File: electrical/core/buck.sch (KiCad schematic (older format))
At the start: 0 parts

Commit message: Size SEPIC inductor and MOSFETs
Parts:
- added L1: 15u, symbol Device:L
- added Q3, Q4: IRF540N, Package_TO_SOT_THT:TO-220-3_Vertical, symbol Transistor_FET:IRF540N
- added U5: LM5118, Package_SO:HTSSOP-20-1EP_4.4x6.5mm_P0.65mm_EP3.4x6.5mm, symbol rasbot:LM5118
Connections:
- new net: Q4.1 (G), U5.15 (LO)
- new net: Q3.1 (G), U5.19 (HO)
- new net: L1.1, Q3.3 (S), U5.20 (HS)
- new net: L1.2, Q4.2 (D)
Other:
- note added: "SEPIC"
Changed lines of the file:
@@
 Comment4 ""
 $EndDescr
+Text Notes 2650 2850 0    100  ~ 20
+SEPIC
+$Comp
+L rasbot:LM5118 U5
+U 1 1 5D54082F
+P 2700 4100
+F 0 "U5" H 2700 4993 100 0000 C CNN
+F 1 "LM5118" H 2700 4827 100 0000 C CNN
+F 2 "Package_SO:HTSSOP-20-1EP_4.4x6.5mm_P0.65mm_EP3.4x6.5mm" H 2600 4000 100 0001 C CNN
+F 3 "http://www.ti.com/lit/ds/symlink/lm5118.pdf" H 2600 4000 100 0001 C CNN
+	1    2700 4100
+	1    0    0    -1
+$EndComp
+$Comp
+L Transistor_FET:IRF540N Q4
+U 1 1 5D541C10
+P 4750 4400
+F 0 "Q4" H 4956 4446 50  0000 L CNN
+F 1 "IRF540N" H 4956 4355 50  0000 L CNN
+F 2 "Package_TO_SOT_THT:TO-220-3_Vertical" H 5000 4325 50  0001 L CIN
+F 3 "http://www.irf.com/product-info/datasheets/data/irf540n.pdf" H 4750 4400 50  0001 L CNN
+	1    4750 4400
+	1    0    0    -1
+$EndComp
+Wire Wire Line
+	4550 4400 3200 4400
+Wire Wire Line
+	3200 4000 3250 4000
+$Comp
+L Device:L L1
+U 1 1 5D54429F
+P 4600 4100
+F 0 "L1" V 4790 4100 50  0000 C CNN
+F 1 "15u" V 4699 4100 50  0000 C CNN
+F 2 "" H 4600 4100 50  0001 C CNN
+F 3 "~" H 4600 4100 50  0001 C CNN
+	1    4600 4100
+	0    -1   -1   0
+$EndComp
+Wire Wire Line
+	4750 4100 4850 4100
+Wire Wire Line
+	4850 4100 4850 4200
+Wire Wire Line
+	3250 4000 3250 4100
+Connection ~ 4000 4100
+Wire Wire Line
+	3250 4100 4000 4100
+Wire Wire Line
+	4450 4100 4000 4100
+Wire Wire Line
+	3700 3900 3200 3900
+$Comp
+L Transistor_FET:IRF540N Q3
+U 1 1 5D54261D
+P 3900 3900
+F 0 "Q3" H 4106 3946 50  0000 L CNN
+F 1 "IRF540N" H 4106 3855 50  0000 L CNN
+F 2 "Package_TO_SOT_THT:TO-220-3_Vertical" H 4150 3825 50  0001 L CIN
+F 3 "http://www.irf.com/product-info/datasheets/data/irf540n.pdf" H 3900 3900 50  0001 L CNN
+	1    3900 3900
+	1    0    0    -1
+$EndComp
 $EndSCHEMATC

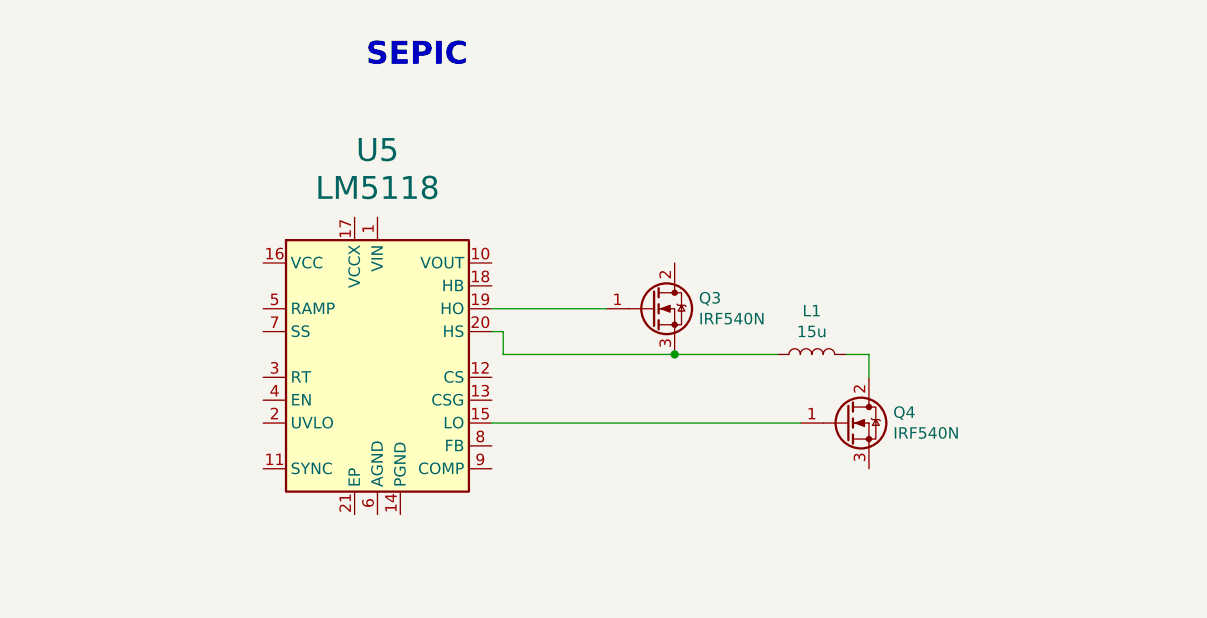
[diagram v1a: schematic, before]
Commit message: Fix division in power
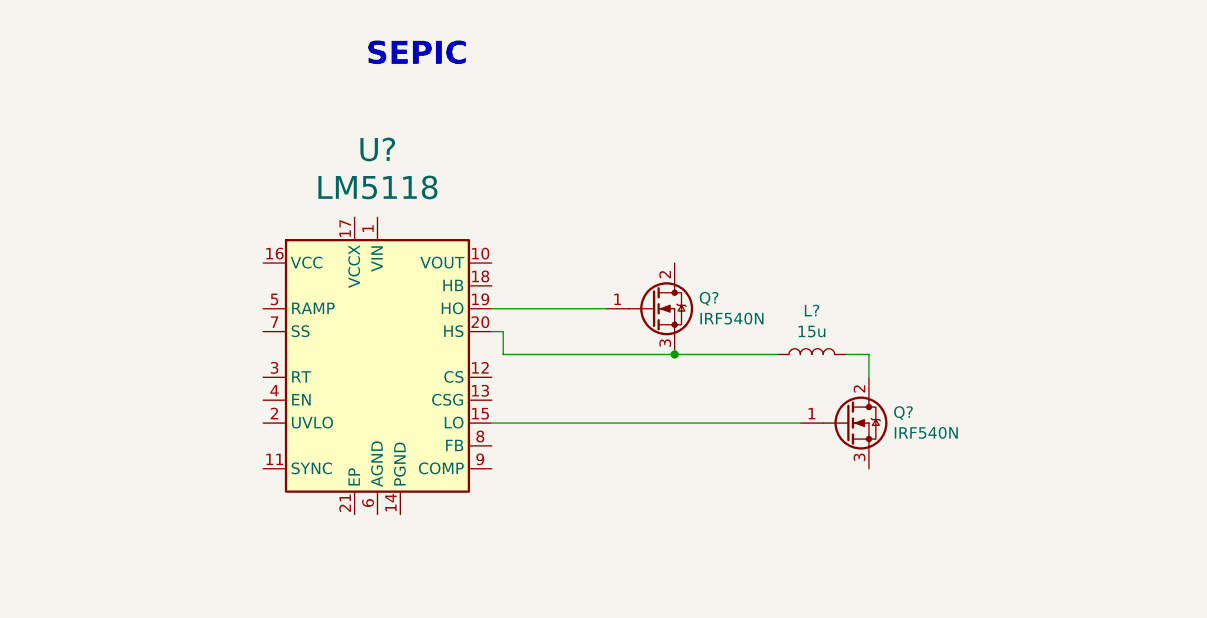
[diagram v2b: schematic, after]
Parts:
- renumbered L1 to L?, Q4 to Q?, Q3 to Q?, U5 to U?
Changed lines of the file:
@@
 SEPIC
 $Comp
-L rasbot:LM5118 U5
+L rasbot:LM5118 U?
 U 1 1 5D54082F
 P 2700 4100
-F 0 "U5" H 2700 4993 100 0000 C CNN
+F 0 "U?" H 2700 4993 100 0000 C CNN
 F 1 "LM5118" H 2700 4827 100 0000 C CNN
 F 2 "Package_SO:HTSSOP-20-1EP_4.4x6.5mm_P0.65mm_EP3.4x6.5mm" H 2600 4000 100 0001 C CNN
@@
 $EndComp
 $Comp
-L Transistor_FET:IRF540N Q4
+L Transistor_FET:IRF540N Q?
 U 1 1 5D541C10
 P 4750 4400
-F 0 "Q4" H 4956 4446 50  0000 L CNN
+F 0 "Q?" H 4956 4446 50  0000 L CNN
 F 1 "IRF540N" H 4956 4355 50  0000 L CNN
 F 2 "Package_TO_SOT_THT:TO-220-3_Vertical" H 5000 4325 50  0001 L CIN
@@
 	3200 4000 3250 4000
 $Comp
-L Device:L L1
+L Device:L L?
 U 1 1 5D54429F
 P 4600 4100
-F 0 "L1" V 4790 4100 50  0000 C CNN
+F 0 "L?" V 4790 4100 50  0000 C CNN
 F 1 "15u" V 4699 4100 50  0000 C CNN
 F 2 "" H 4600 4100 50  0001 C CNN
@@
 	3700 3900 3200 3900
 $Comp
-L Transistor_FET:IRF540N Q3
+L Transistor_FET:IRF540N Q?
 U 1 1 5D54261D
 P 3900 3900
-F 0 "Q3" H 4106 3946 50  0000 L CNN
+F 0 "Q?" H 4106 3946 50  0000 L CNN
 F 1 "IRF540N" H 4106 3855 50  0000 L CNN
 F 2 "Package_TO_SOT_THT:TO-220-3_Vertical" H 4150 3825 50  0001 L CIN

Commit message: Supply and Enable
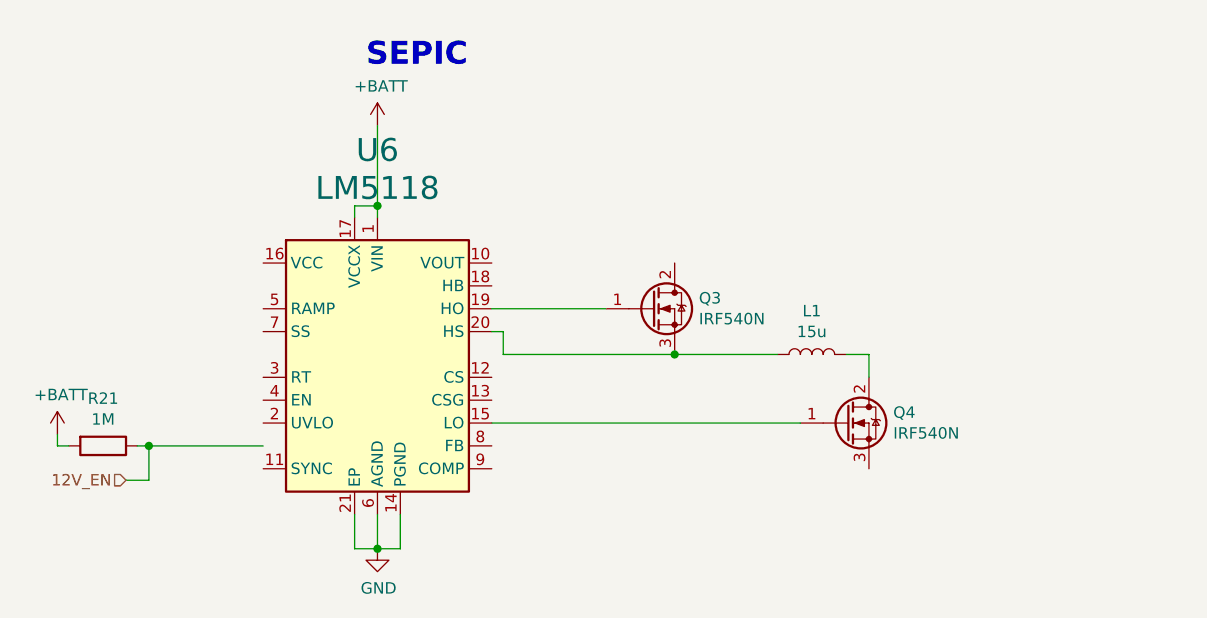
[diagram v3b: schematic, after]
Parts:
- added R21: 1M, symbol Device:R
- gave numbers to parts that had none: 4
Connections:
- net labels added: +BATT, 12V_EN, GND
- wire segments 8 -> 23
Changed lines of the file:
@@
 SEPIC
 $Comp
-L rasbot:LM5118 U?
+L rasbot:LM5118 U6
 U 1 1 5D54082F
 P 2700 4100
-F 0 "U?" H 2700 4993 100 0000 C CNN
+F 0 "U6" H 2700 4993 100 0000 C CNN
 F 1 "LM5118" H 2700 4827 100 0000 C CNN
 F 2 "Package_SO:HTSSOP-20-1EP_4.4x6.5mm_P0.65mm_EP3.4x6.5mm" H 2600 4000 100 0001 C CNN
@@
 $EndComp
 $Comp
-L Transistor_FET:IRF540N Q?
+L Transistor_FET:IRF540N Q4
 U 1 1 5D541C10
 P 4750 4400
-F 0 "Q?" H 4956 4446 50  0000 L CNN
+F 0 "Q4" H 4956 4446 50  0000 L CNN
 F 1 "IRF540N" H 4956 4355 50  0000 L CNN
 F 2 "Package_TO_SOT_THT:TO-220-3_Vertical" H 5000 4325 50  0001 L CIN
@@
 	3200 4000 3250 4000
 $Comp
-L Device:L L?
+L Device:L L1
 U 1 1 5D54429F
 P 4600 4100
-F 0 "L?" V 4790 4100 50  0000 C CNN
+F 0 "L1" V 4790 4100 50  0000 C CNN
 F 1 "15u" V 4699 4100 50  0000 C CNN
 F 2 "" H 4600 4100 50  0001 C CNN
@@
 	3700 3900 3200 3900
 $Comp
-L Transistor_FET:IRF540N Q?
+L Transistor_FET:IRF540N Q3
 U 1 1 5D54261D
 P 3900 3900
-F 0 "Q?" H 4106 3946 50  0000 L CNN
+F 0 "Q3" H 4106 3946 50  0000 L CNN
 F 1 "IRF540N" H 4106 3855 50  0000 L CNN
 F 2 "Package_TO_SOT_THT:TO-220-3_Vertical" H 4150 3825 50  0001 L CIN
@@
 	1    0    0    -1
 $EndComp
+$Comp
+L power:+BATT #PWR?
+U 1 1 5DA92B89
+P 2700 3100
+AR Path="/5D48851F/5DA878D9/5DA92B89" Ref="#PWR?"  Part="1"
+AR Path="/5D48851F/5DA8C423/5DA92B89" Ref="#PWR051"  Part="1"
+F 0 "#PWR051" H 2700 2950 50  0001 C CNN
+F 1 "+BATT" H 2715 3273 50  0000 C CNN
+F 2 "" H 2700 3100 50  0001 C CNN
+F 3 "" H 2700 3100 50  0001 C CNN
+	1    2700 3100
+	1    0    0    -1
+$EndComp
+Wire Wire Line
+	2700 3100 2700 3450
+Wire Wire Line
+	2700 3450 2600 3450
+Wire Wire Line
+	2600 3450 2600 3500
+Connection ~ 2700 3450
+Wire Wire Line
+	2700 3450 2700 3500
+$Comp
+L power:GND #PWR052
+U 1 1 5DA9483F
+P 2700 4950
+F 0 "#PWR052" H 2700 4700 50  0001 C CNN
+F 1 "GND" H 2705 4777 50  0000 C CNN
+F 2 "" H 2700 4950 50  0001 C CNN
+F 3 "" H 2700 4950 50  0001 C CNN
+	1    2700 4950
+	1    0    0    -1
+$EndComp
+Wire Wire Line
+	2700 4950 2600 4950
+Wire Wire Line
+	2600 4950 2600 4800
+Wire Wire Line
+	2700 4950 2800 4950
+Wire Wire Line
+	2800 4950 2800 4800
+Connection ~ 2700 4950
+Wire Wire Line
+	2700 4950 2700 4800
+$Comp
+L Device:R R21
+U 1 1 5DA95D12
+P 1500 4500
+F 0 "R21" V 1293 4500 50  0000 C CNN
+F 1 "1M" V 1384 4500 50  0000 C CNN
+F 2 "" V 1430 4500 50  0001 C CNN
+F 3 "~" H 1500 4500 50  0001 C CNN
+	1    1500 4500
+	0    1    1    0
+$EndComp
+$Comp
+L power:+BATT #PWR?
+U 1 1 5DA97039
+P 1300 4450
+AR Path="/5D48851F/5DA878D9/5DA97039" Ref="#PWR?"  Part="1"
+AR Path="/5D48851F/5DA8C423/5DA97039" Ref="#PWR050"  Part="1"
+F 0 "#PWR050" H 1300 4300 50  0001 C CNN
+F 1 "+BATT" H 1315 4623 50  0000 C CNN
+F 2 "" H 1300 4450 50  0001 C CNN
+F 3 "" H 1300 4450 50  0001 C CNN
+	1    1300 4450
+	1    0    0    -1
+$EndComp
+Wire Wire Line
+	1300 4450 1300 4500
+Wire Wire Line
+	1300 4500 1350 4500
+Wire Wire Line
+	1650 4500 1700 4500
+Text HLabel 1600 4650 0    50   Input ~ 0
+12V_EN
+Wire Wire Line
+	1600 4650 1700 4650
+Wire Wire Line
+	1700 4650 1700 4500
+Connection ~ 1700 4500
+Wire Wire Line
+	1700 4500 2200 4500
 $EndSCHEMATC

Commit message: Inductor Footprint
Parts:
- L1: footprint (none) -> Inductor_SMD:L_10.4x10.4_H4.8
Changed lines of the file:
@@
 F 0 "L1" V 4790 4100 50  0000 C CNN
 F 1 "15u" V 4699 4100 50  0000 C CNN
-F 2 "" H 4600 4100 50  0001 C CNN
+F 2 "Inductor_SMD:L_10.4x10.4_H4.8" H 4600 4100 50  0001 C CNN
 F 3 "~" H 4600 4100 50  0001 C CNN
 	1    4600 4100

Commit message: MOSFET Footprint
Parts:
- Q3, Q4: footprint Package_TO_SOT_THT:TO-220-3_Vertical -> Package_TO_SOT_SMD:TO-263-2
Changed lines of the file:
@@
 F 0 "Q4" H 4956 4446 50  0000 L CNN
 F 1 "IRF540N" H 4956 4355 50  0000 L CNN
-F 2 "Package_TO_SOT_THT:TO-220-3_Vertical" H 5000 4325 50  0001 L CIN
+F 2 "Package_TO_SOT_SMD:TO-263-2" H 5000 4325 50  0001 L CIN
 F 3 "http://www.irf.com/product-info/datasheets/data/irf540n.pdf" H 4750 4400 50  0001 L CNN
 	1    4750 4400
@@
 F 0 "Q3" H 4106 3946 50  0000 L CNN
 F 1 "IRF540N" H 4106 3855 50  0000 L CNN
-F 2 "Package_TO_SOT_THT:TO-220-3_Vertical" H 4150 3825 50  0001 L CIN
+F 2 "Package_TO_SOT_SMD:TO-263-2" H 4150 3825 50  0001 L CIN
 F 3 "http://www.irf.com/product-info/datasheets/data/irf540n.pdf" H 3900 3900 50  0001 L CNN
 	1    3900 3900

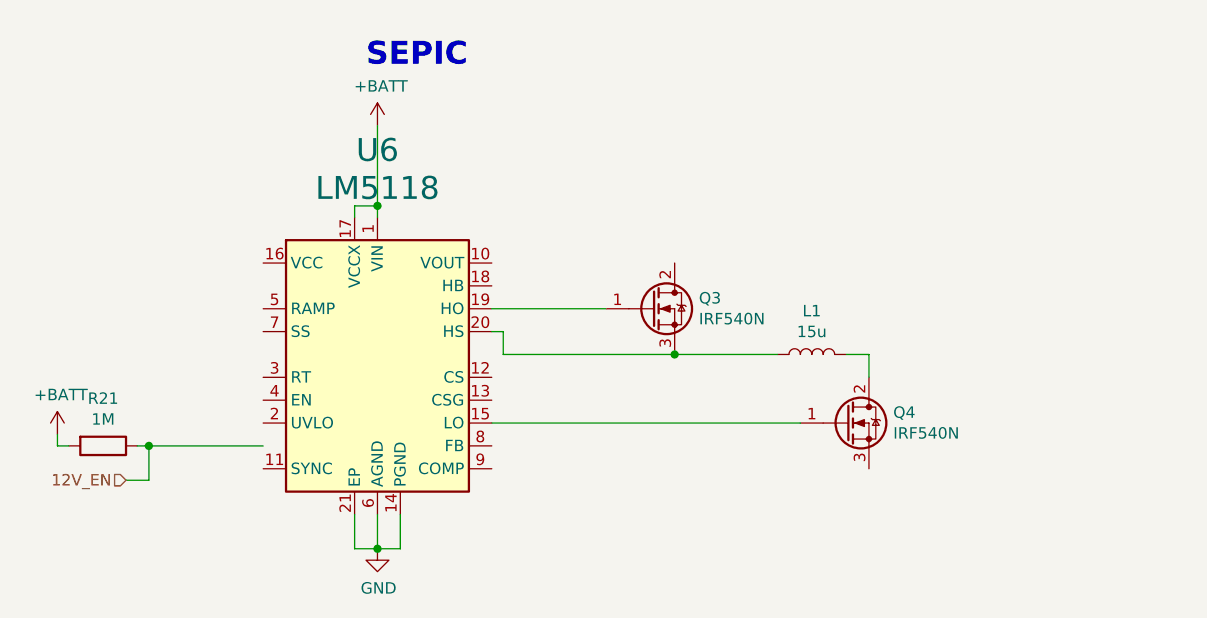
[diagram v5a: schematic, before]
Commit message: SEPIC rectify output
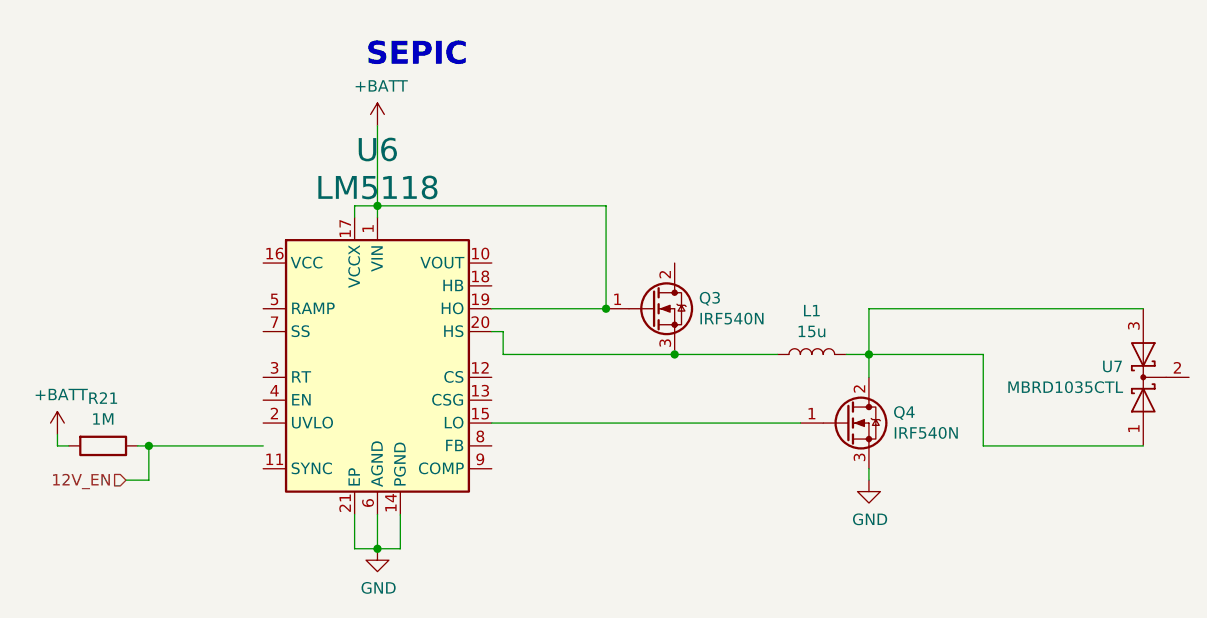
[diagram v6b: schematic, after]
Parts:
- added U7: MBRD1035CTL, symbol rasbot:MBRD1035CTL
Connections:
- wire segments 23 -> 31
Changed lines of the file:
@@
 Wire Wire Line
 	4450 4100 4000 4100
-Wire Wire Line
-	3700 3900 3200 3900
 $Comp
 L Transistor_FET:IRF540N Q3
@@
 Wire Wire Line
 	2700 3100 2700 3450
-Wire Wire Line
-	2700 3450 2600 3450
-Wire Wire Line
-	2600 3450 2600 3500
 Connection ~ 2700 3450
 Wire Wire Line
@@
 Wire Wire Line
 	1700 4500 2200 4500
+Wire Wire Line
+	3700 3900 3700 3450
+Wire Wire Line
+	3700 3450 2700 3450
+Connection ~ 3700 3900
+Wire Wire Line
+	3700 3900 3200 3900
+$Comp
+L power:GND #PWR053
+U 1 1 5DAA46C0
+P 4850 4650
+F 0 "#PWR053" H 4850 4400 50  0001 C CNN
+F 1 "GND" H 4855 4477 50  0000 C CNN
+F 2 "" H 4850 4650 50  0001 C CNN
+F 3 "" H 4850 4650 50  0001 C CNN
+	1    4850 4650
+	1    0    0    -1
+$EndComp
+Wire Wire Line
+	4850 4650 4850 4600
+Wire Wire Line
+	2600 3450 2600 3500
+Wire Wire Line
+	2700 3450 2600 3450
+$Comp
+L rasbot:MBRD1035CTL U7
+U 1 1 5DAAF97C
+P 6050 4200
+F 0 "U7" V 6096 4288 50  0000 L CNN
+F 1 "MBRD1035CTL" V 6005 4288 50  0000 L CNN
+F 2 "" H 6050 4200 50  0001 C CNN
+F 3 "" H 6050 4200 50  0001 C CNN
+	1    6050 4200
+	0    -1   -1   0
+$EndComp
+Wire Wire Line
+	6050 3900 4850 3900
+Wire Wire Line
+	4850 3900 4850 4100
+Connection ~ 4850 4100
+Wire Wire Line
+	6050 4500 5350 4500
+Wire Wire Line
+	5350 4500 5350 4100
+Wire Wire Line
+	5350 4100 4850 4100
 $EndSCHEMATC

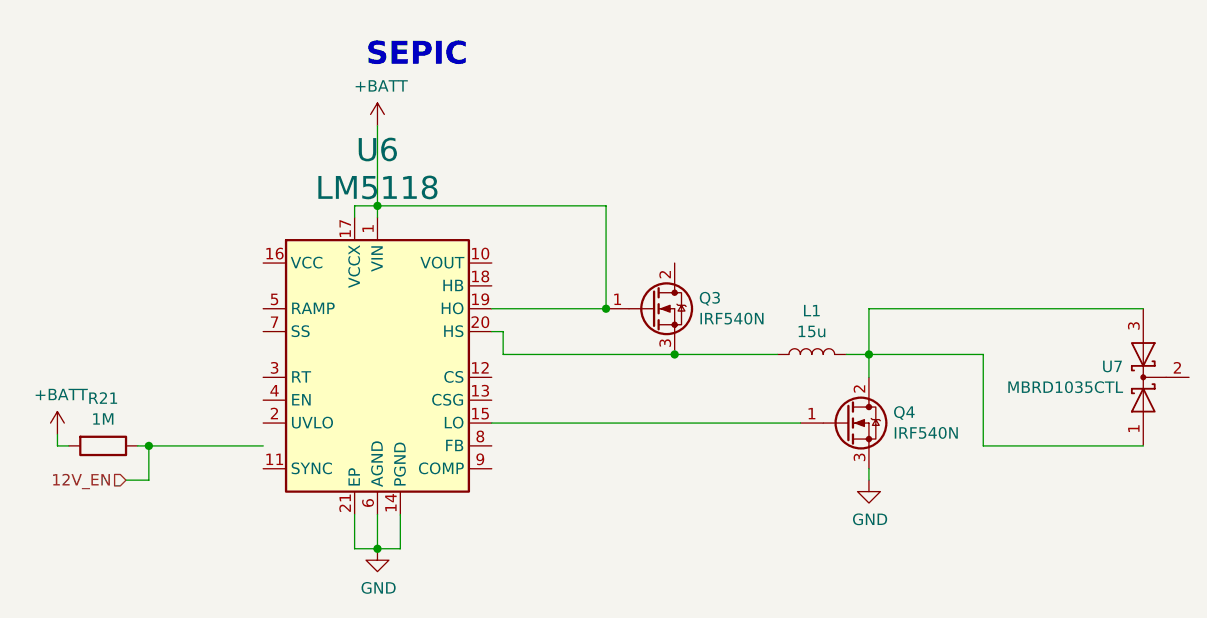
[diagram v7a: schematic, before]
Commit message: Fix connection to Vin
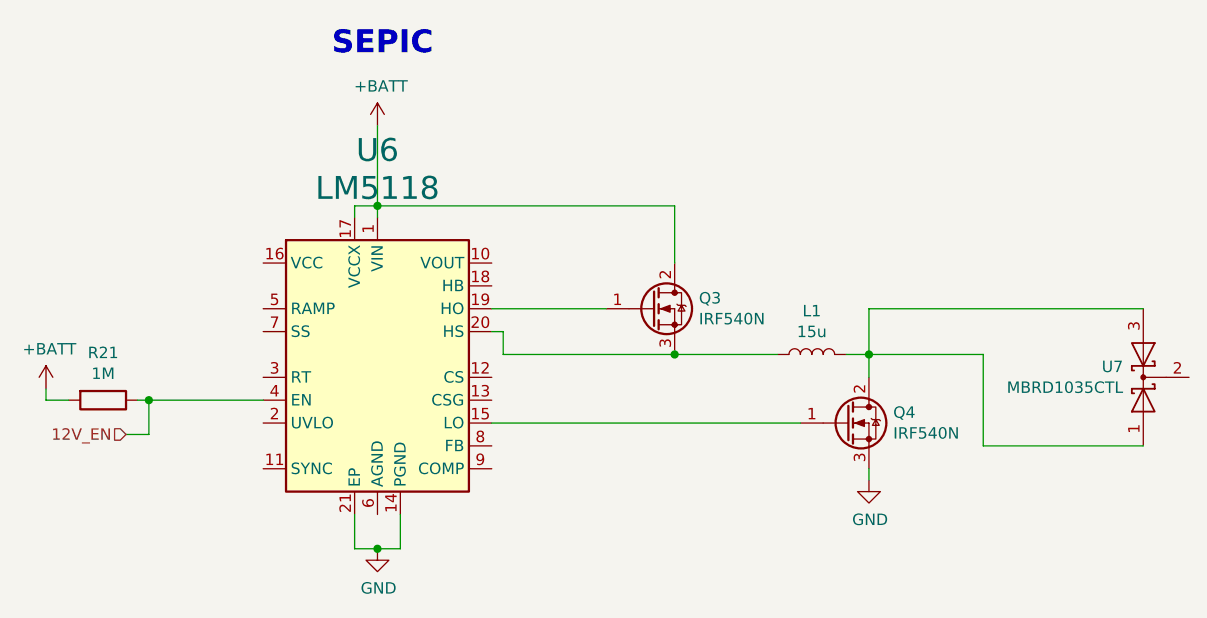
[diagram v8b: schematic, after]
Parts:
- U7: footprint (none) -> Package_TO_SOT_SMD:TO-252-2
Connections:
- wire segments 31 -> 30
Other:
- moved on the sheet: R21
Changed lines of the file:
@@
 EESchema Schematic File Version 4
-LIBS:core-cache
-EELAYER 26 0
+EELAYER 30 0
 EELAYER END
 $Descr A4 11693 8268
@@
 Comment4 ""
 $EndDescr
-Text Notes 2650 2850 0    100  ~ 20
+Text Notes 2500 2800 0    100  ~ 20
 SEPIC
 $Comp
@@
 	2800 4950 2800 4800
 Connection ~ 2700 4950
-Wire Wire Line
-	2700 4950 2700 4800
 $Comp
 L Device:R R21
 U 1 1 5DA95D12
-P 1500 4500
-F 0 "R21" V 1293 4500 50  0000 C CNN
-F 1 "1M" V 1384 4500 50  0000 C CNN
-F 2 "" V 1430 4500 50  0001 C CNN
-F 3 "~" H 1500 4500 50  0001 C CNN
-	1    1500 4500
+P 1500 4300
+F 0 "R21" V 1293 4300 50  0000 C CNN
+F 1 "1M" V 1384 4300 50  0000 C CNN
+F 2 "" V 1430 4300 50  0001 C CNN
+F 3 "~" H 1500 4300 50  0001 C CNN
+	1    1500 4300
 	0    1    1    0
 $EndComp
@@
 L power:+BATT #PWR?
 U 1 1 5DA97039
-P 1300 4450
+P 1250 4250
 AR Path="/5D48851F/5DA878D9/5DA97039" Ref="#PWR?"  Part="1"
 AR Path="/5D48851F/5DA8C423/5DA97039" Ref="#PWR050"  Part="1"
-F 0 "#PWR050" H 1300 4300 50  0001 C CNN
-F 1 "+BATT" H 1315 4623 50  0000 C CNN
-F 2 "" H 1300 4450 50  0001 C CNN
-F 3 "" H 1300 4450 50  0001 C CNN
-	1    1300 4450
+F 0 "#PWR050" H 1250 4100 50  0001 C CNN
+F 1 "+BATT" H 1265 4423 50  0000 C CNN
+F 2 "" H 1250 4250 50  0001 C CNN
+F 3 "" H 1250 4250 50  0001 C CNN
+	1    1250 4250
 	1    0    0    -1
 $EndComp
 Wire Wire Line
-	1300 4450 1300 4500
+	1250 4250 1250 4300
 Wire Wire Line
-	1300 4500 1350 4500
+	1250 4300 1350 4300
 Wire Wire Line
-	1650 4500 1700 4500
-Text HLabel 1600 4650 0    50   Input ~ 0
+	1650 4300 1700 4300
+Text HLabel 1600 4450 0    50   Input ~ 0
 12V_EN
 Wire Wire Line
-	1600 4650 1700 4650
+	1600 4450 1700 4450
 Wire Wire Line
-	1700 4650 1700 4500
-Connection ~ 1700 4500
+	1700 4450 1700 4300
+Connection ~ 1700 4300
 Wire Wire Line
-	1700 4500 2200 4500
-Wire Wire Line
-	3700 3900 3700 3450
-Wire Wire Line
-	3700 3450 2700 3450
-Connection ~ 3700 3900
+	1700 4300 2200 4300
 Wire Wire Line
 	3700 3900 3200 3900
@@
 F 0 "U7" V 6096 4288 50  0000 L CNN
 F 1 "MBRD1035CTL" V 6005 4288 50  0000 L CNN
-F 2 "" H 6050 4200 50  0001 C CNN
+F 2 "Package_TO_SOT_SMD:TO-252-2" H 6050 4200 50  0001 C CNN
 F 3 "" H 6050 4200 50  0001 C CNN
 	1    6050 4200
@@
 Wire Wire Line
 	5350 4100 4850 4100
+Wire Wire Line
+	4000 3450 4000 3700
+Wire Wire Line
+	2700 3450 4000 3450
 $EndSCHEMATC
